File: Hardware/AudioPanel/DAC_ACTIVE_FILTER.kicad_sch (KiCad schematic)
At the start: 20 parts, among them U107 AD8606ARM, U108 AD8606ARM

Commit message: small stuff
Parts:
- renumbered C474 to C201, C476 to C202, C477 to C203, C478 to C204, C479 to C205, C480 to C206, C481 to C207, C482 to C208, C483 to C209, C484 to C210, R306 to R218, R308 to R219, R309 to R220, R310 to R221, R311 to R222, R312 to R223, R313 to R224, R314 to R225, U108 to U60, U107 to U60, U108 to U61

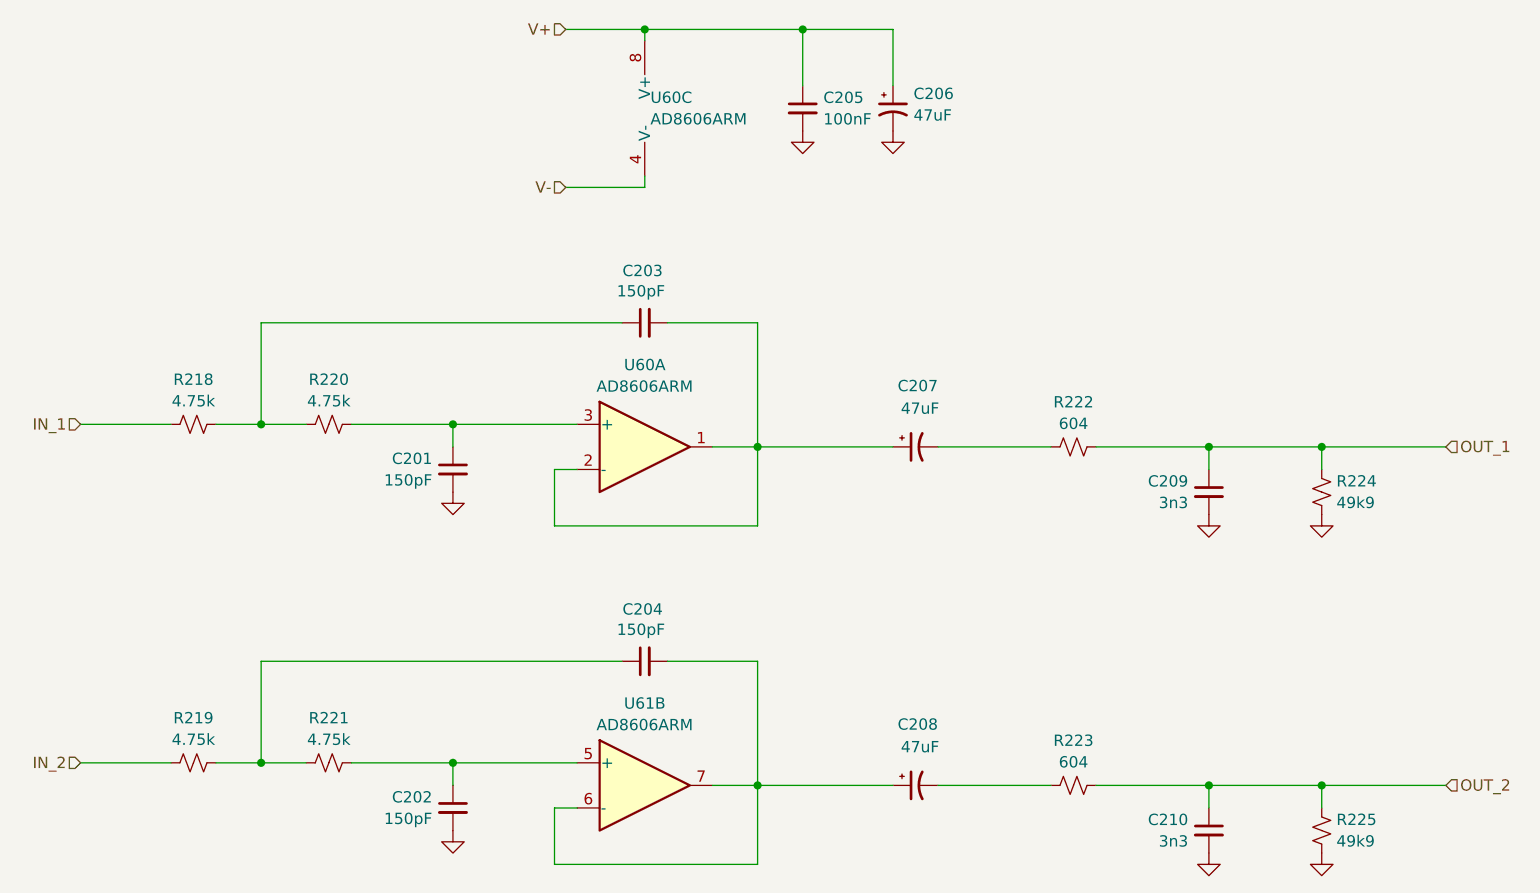
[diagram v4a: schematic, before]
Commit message: Realized that I need to rethink how I'm going to mix the radio audio with the stereo audio
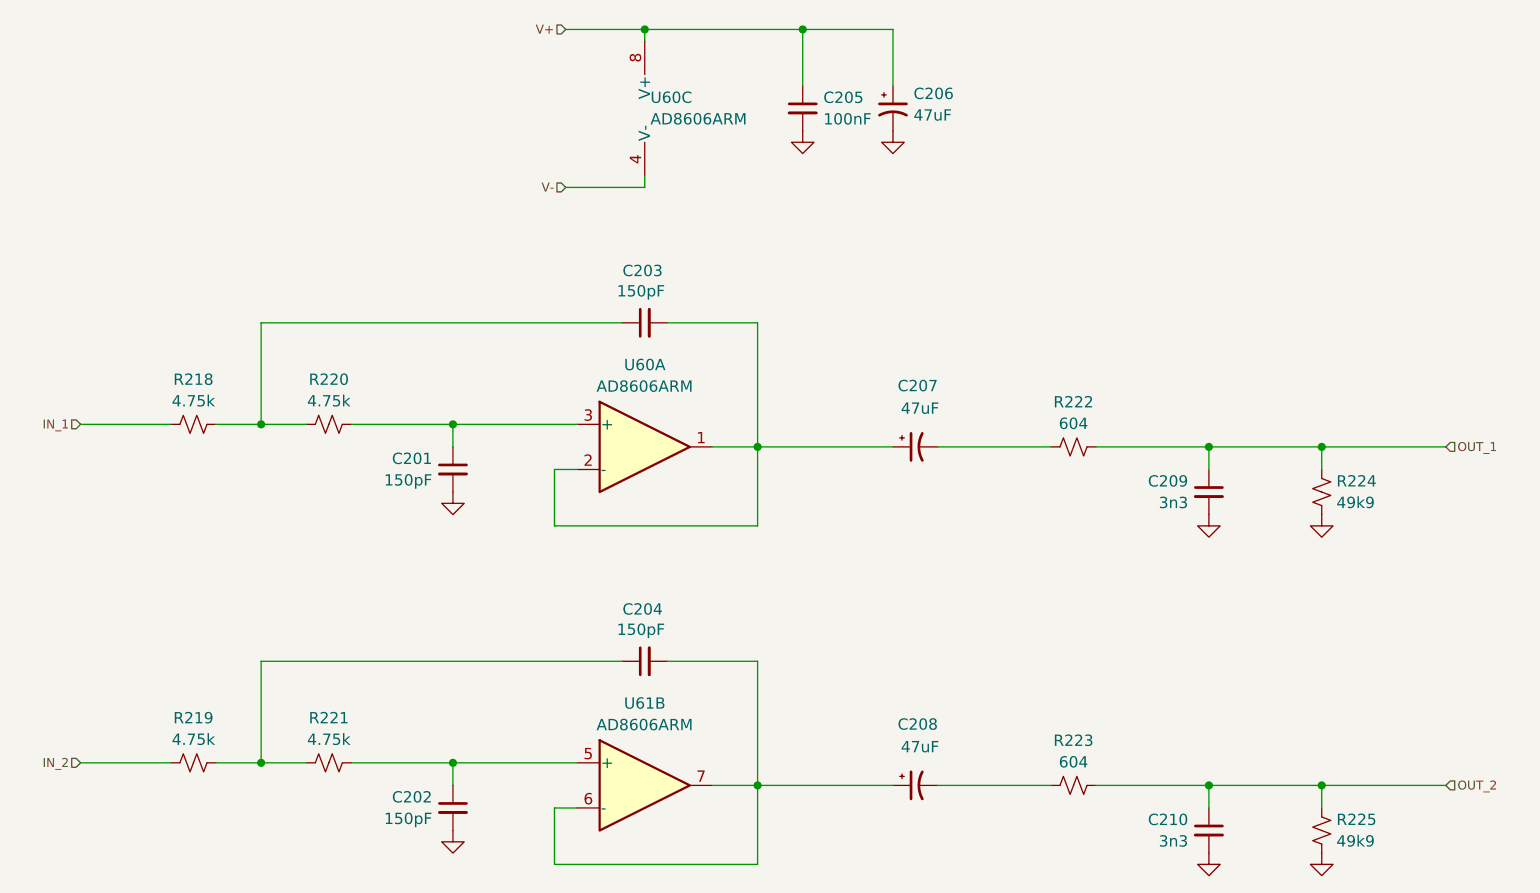
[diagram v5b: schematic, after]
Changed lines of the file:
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@@
 		(effects
 			(font
-				(size 1.27 1.27)
+				(size 1 1)
 			)
 			(justify right)
@@
 		(effects
 			(font
-				(size 1.27 1.27)
+				(size 1 1)
 			)
 			(justify right)
@@
 		(effects
 			(font
-				(size 1.27 1.27)
+				(size 1 1)
 			)
 			(justify right)
@@
 		(effects
 			(font
-				(size 1.27 1.27)
+				(size 1 1)
 			)
 			(justify left)
@@
 		(effects
 			(font
-				(size 1.27 1.27)
+				(size 1 1)
 			)
 			(justify right)
@@
 		(effects
 			(font
-				(size 1.27 1.27)
+				(size 1 1)
 			)
 			(justify left)

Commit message: Added MT8816 for audio switching
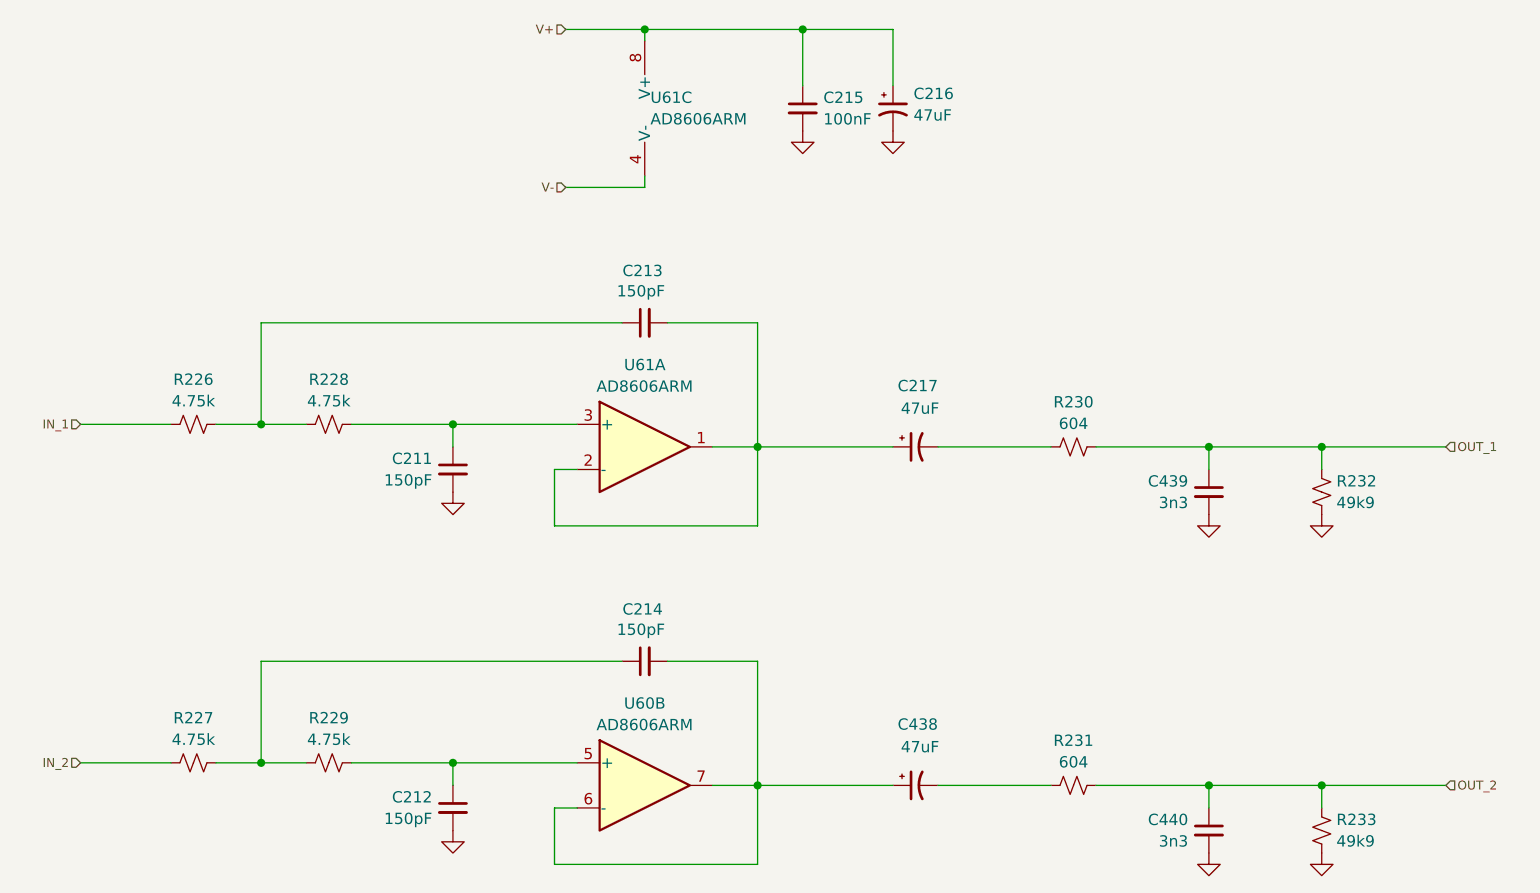
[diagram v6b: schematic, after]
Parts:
- renumbered C201 to C211, C202 to C212, C203 to C213, C204 to C214, C205 to C215, C206 to C216, C207 to C217, C208 to C438, C209 to C439, C210 to C440, R218 to R226, R219 to R227, R220 to R228, R221 to R229, R222 to R230, R223 to R231, R224 to R232, R225 to R233, U61 to U60, U60 to U61
